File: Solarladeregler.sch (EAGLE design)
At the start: 75 parts, among them CON1 FLATFLEX, IC1 MWL_LT3652LT3652, IC2 LTC3428, IC3 LTC6102, IC4 LTC6102, IC5 TSIC206, Q1 MOSFET, Q2 BSS138, X1 PN87520-S

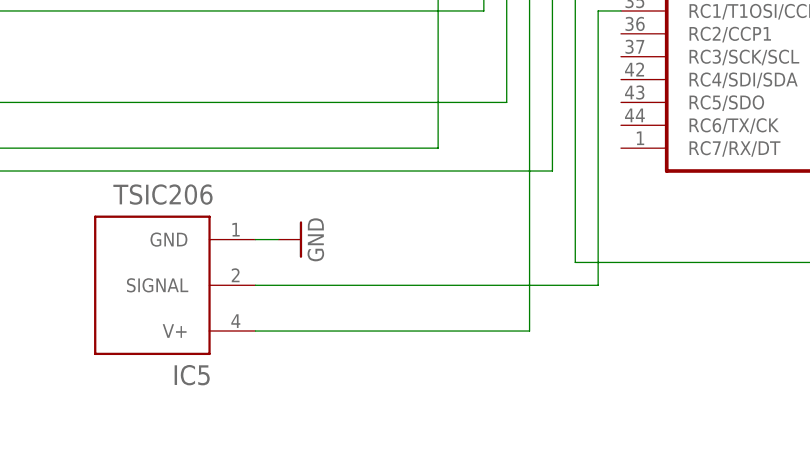
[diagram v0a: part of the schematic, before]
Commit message: TSIC 206
resistor +capacitor
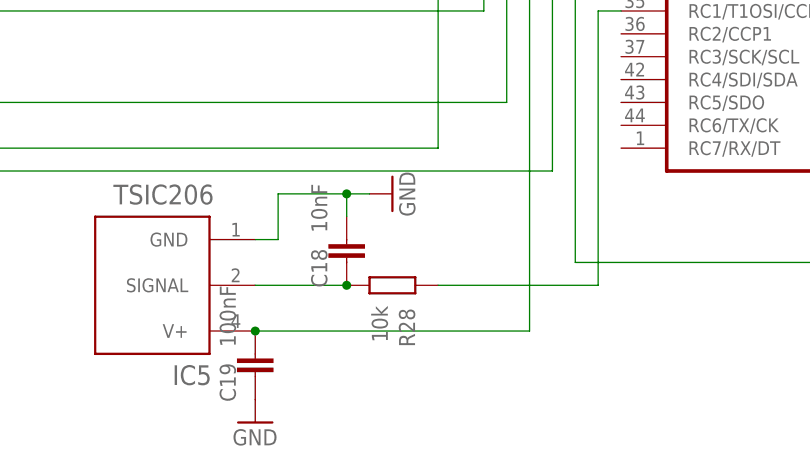
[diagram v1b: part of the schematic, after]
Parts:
- added C18: 10nF, rcl:C-EUC0805
- added C19: 100nF, rcl:C-EUC0805
- added R28: 10k, rcl:R-EU_R0805
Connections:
- new net N$53: C18.2, IC5.SIGNAL, R28.2
- net GND: now also C18.1, C19.2
- net N$50: now also R28.1; no longer IC5.SIGNAL
- net N$52: now also C19.1
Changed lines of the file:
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@@
 <?xml version="1.0" encoding="utf-8"?>
 <!DOCTYPE eagle SYSTEM "eagle.dtd">
-<eagle version="6.3">
+<eagle version="6.4">
 <drawing>
 <settings>
@@
 <setting verticaltext="up"/>
 </settings>
-<grid distance="0.1" unitdist="inch" unit="inch" style="lines" multiple="1" display="no" altdistance="0.01" altunitdist="inch" altunit="inch"/>
+<grid distance="0.1" unitdist="inch" unit="mm" style="dots" multiple="1" display="yes" altdistance="0.01" altunitdist="inch" altunit="mm"/>
 <layers>
 <layer number="1" name="Top" color="4" fill="1" visible="no" active="no"/>
@@
 <part name="IC5" library="linear" deviceset="TSIC206" device=""/>
 <part name="GND26" library="supply1" deviceset="GND" device=""/>
+<part name="R28" library="rcl" deviceset="R-EU_" device="R0805" value="10k"/>
+<part name="C18" library="rcl" deviceset="C-EU" device="C0805" value="10nF"/>
+<part name="C19" library="rcl" deviceset="C-EU" device="C0805" value="100nF"/>
+<part name="GND27" library="supply1" deviceset="GND" device=""/>
 </parts>
 <sheets>
@@
 </instance>
 <instance part="IC5" gate="G$1" x="342.9" y="0" rot="R180"/>
-<instance part="GND26" gate="1" x="345.44" y="-2.54" smashed="yes" rot="R90">
-<attribute name="VALUE" x="347.98" y="-5.08" size="1.778" layer="96" rot="R90"/>
+<instance part="GND26" gate="1" x="355.6" y="2.54" smashed="yes" rot="R90">
+<attribute name="VALUE" x="358.14" y="0" size="1.778" layer="96" rot="R90"/>
+</instance>
+<instance part="R28" gate="G$1" x="355.6" y="-7.62" smashed="yes" rot="R180">
+<attribute name="NAME" x="356.3366" y="-10.16" size="1.778" layer="95" rot="R270"/>
+<attribute name="VALUE" x="353.314" y="-9.906" size="1.778" layer="96" rot="R270"/>
+</instance>
+<instance part="C18" gate="G$1" x="350.52" y="-2.54" smashed="yes">
+<attribute name="NAME" x="348.361" y="-7.874" size="1.778" layer="95" rot="R90"/>
+<attribute name="VALUE" x="348.361" y="-1.778" size="1.778" layer="96" rot="R90"/>
+</instance>
+<instance part="C19" gate="G$1" x="340.36" y="-15.24" smashed="yes">
+<attribute name="NAME" x="338.201" y="-20.574" size="1.778" layer="95" rot="R90"/>
+<attribute name="VALUE" x="338.201" y="-14.478" size="1.778" layer="96" rot="R90"/>
+</instance>
+<instance part="GND27" gate="1" x="340.36" y="-22.86" smashed="yes">
+<attribute name="VALUE" x="337.82" y="-25.4" size="1.778" layer="96"/>
 </instance>
 </instances>
@@
 <segment>
 <pinref part="GND26" gate="1" pin="GND"/>
+<pinref part="C18" gate="G$1" pin="1"/>
+<wire x1="353.06" y1="2.54" x2="350.52" y2="2.54" width="0.1524" layer="91"/>
+<wire x1="350.52" y1="2.54" x2="350.52" y2="0" width="0.1524" layer="91"/>
+<wire x1="350.52" y1="2.54" x2="342.9" y2="2.54" width="0.1524" layer="91"/>
+<wire x1="342.9" y1="2.54" x2="342.9" y2="-2.54" width="0.1524" layer="91"/>
+<junction x="350.52" y="2.54"/>
 <pinref part="IC5" gate="G$1" pin="GND"/>
 <wire x1="342.9" y1="-2.54" x2="340.36" y2="-2.54" width="0.1524" layer="91"/>
+</segment>
+<segment>
+<pinref part="C19" gate="G$1" pin="2"/>
+<pinref part="GND27" gate="1" pin="GND"/>
 </segment>
 </net>
@@
 <net name="N$50" class="0">
 <segment>
-<pinref part="IC5" gate="G$1" pin="SIGNAL"/>
-<wire x1="340.36" y1="-7.62" x2="378.46" y2="-7.62" width="0.1524" layer="91"/>
 <wire x1="378.46" y1="-7.62" x2="378.46" y2="22.86" width="0.1524" layer="91"/>
 <pinref part="µC" gate="_A" pin="RC1/T1OSI/CCP2*"/>
 <wire x1="378.46" y1="22.86" x2="381" y2="22.86" width="0.1524" layer="91"/>
+<pinref part="R28" gate="G$1" pin="1"/>
+<wire x1="360.68" y1="-7.62" x2="378.46" y2="-7.62" width="0.1524" layer="91"/>
 </segment>
 </net>
@@
 <pinref part="µC" gate="_A" pin="RC0/T1OSO/T1CLK"/>
 <wire x1="370.84" y1="25.4" x2="381" y2="25.4" width="0.1524" layer="91"/>
-</segment>
-</net>
+<pinref part="C19" gate="G$1" pin="1"/>
+<junction x="340.36" y="-12.7"/>
+</segment>
+</net>
+<net name="N$53" class="0">
+<segment>
+<pinref part="R28" gate="G$1" pin="2"/>
+<pinref part="IC5" gate="G$1" pin="SIGNAL"/>
+<wire x1="350.52" y1="-7.62" x2="340.36" y2="-7.62" width="0.1524" layer="91"/>
+<pinref part="C18" gate="G$1" pin="2"/>
+<junction x="350.52" y="-7.62"/>
+</segment>
+</net>
